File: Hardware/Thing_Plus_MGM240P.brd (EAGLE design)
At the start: 22.9 x 58.4 mm, 172 parts, among them J1 THING_PLUS_LOGICAL, J2 USB Female Type C Connector, J3 QWIIC_RIGHT_ANGLE, J5 MICRO-SDFRICTION, Q1 20V/4.2A/52mΩ/1.4W, U1 MGM240P, U2 XC6222B331MR-G, U3 EFM32GG12B410F1024GL120, U4 MCP73831, U5 MAX17048, U6 M24C02-FMC6TG, U7 MX25R8035FZUIL0, Y1 CRYSTAL-48MHZ

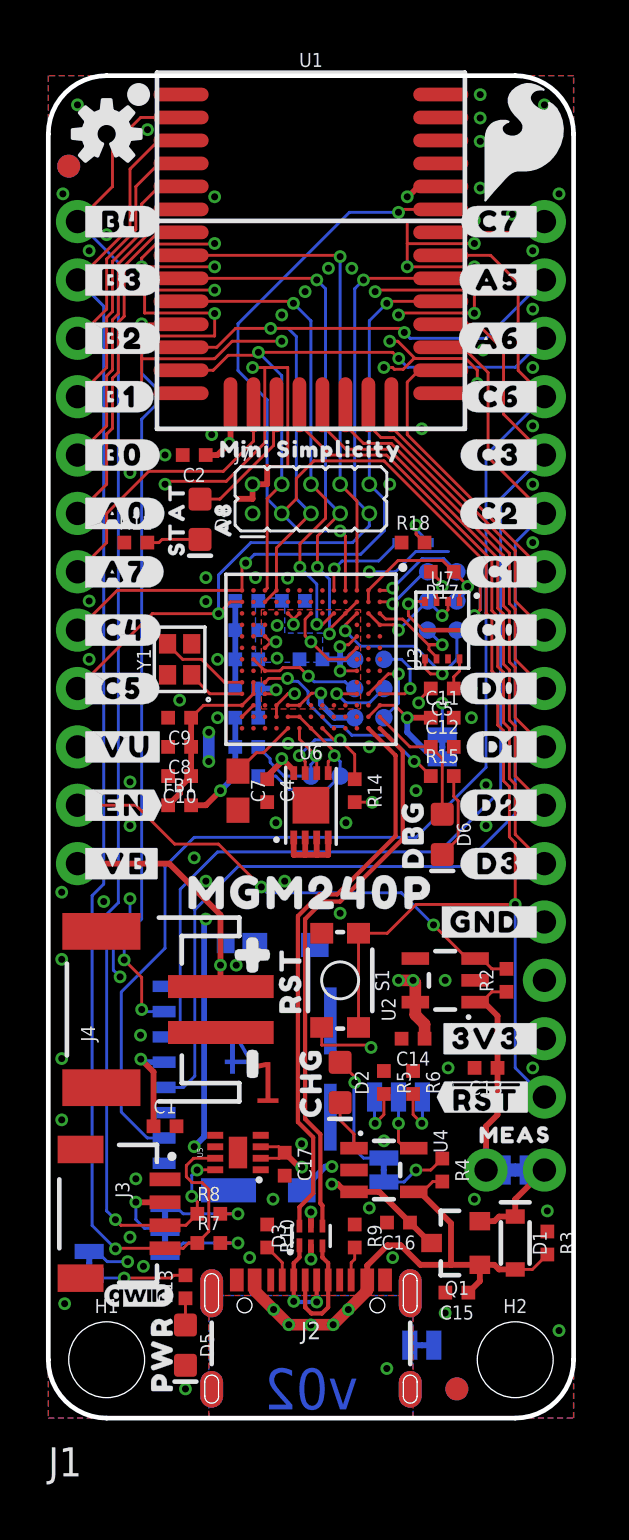
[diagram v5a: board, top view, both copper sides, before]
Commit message: Swap PA04 and PA07
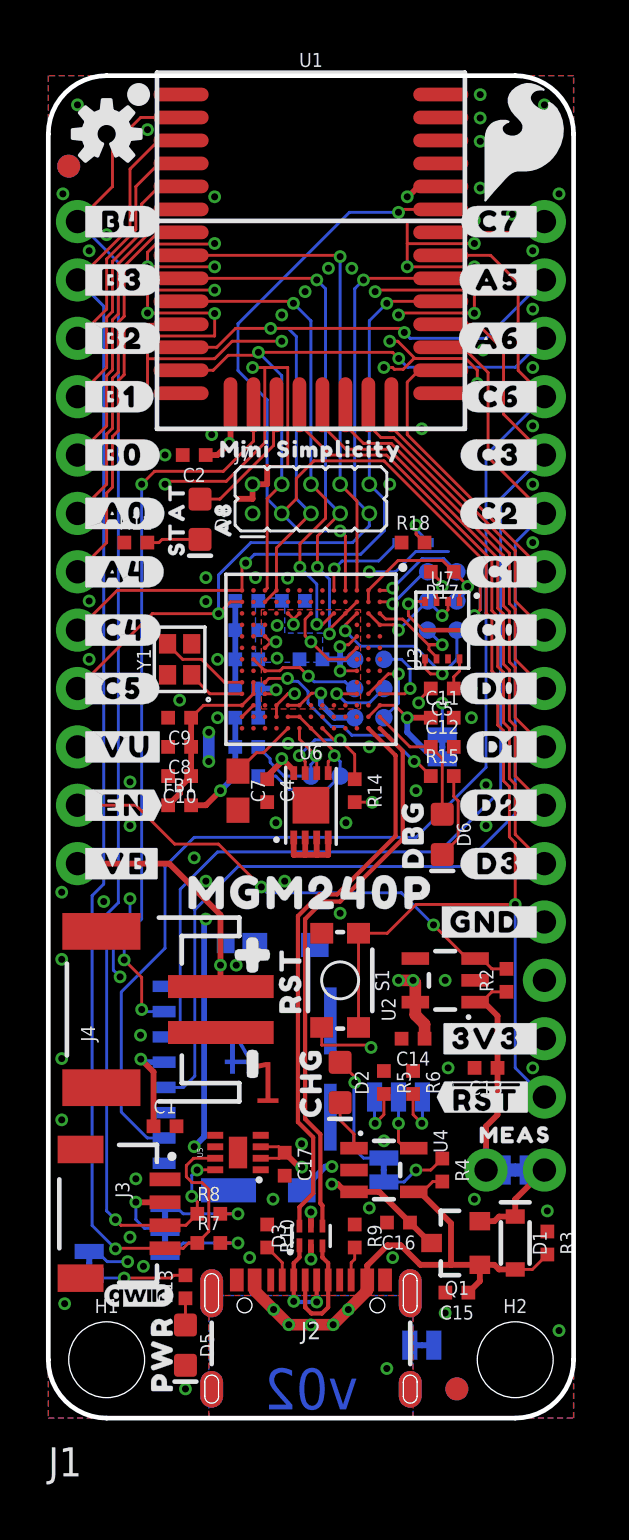
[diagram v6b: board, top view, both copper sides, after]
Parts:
- U$50: device output:#A7_#0 -> output:#A4_#0
- U$8: device output:#_A7#0 -> output:#_A4#0
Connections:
- removed net PA07: J1.7, U1.16
- new net !SD_CS!/PA07: J5.2, U1.16
- net PA04: now also J1.7; no longer J5.2
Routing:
- net !SD_CS!/PA07: track 0.00 -> 31.7 mm, vias 0 -> 3
- net PA04: track 33.7 -> 14.0 mm, vias 3 -> 0
- net PA07: track 12.3 -> 0.00 mm
- net GND: track 120.9 -> 119.9 mm, vias 114 -> 115
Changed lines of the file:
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@@
 <element name="U$6" library="output" package="#_B0#0" value="" x="1.27" y="41.91" smashed="yes"/>
 <element name="U$7" library="output" package="#_A0#0" value="" x="1.27" y="39.37" smashed="yes"/>
-<element name="U$8" library="output" package="#_A7#0" value="" x="1.27" y="36.83" smashed="yes"/>
 <element name="U$9" library="output" package="#_C5#0" value="" x="1.27" y="31.75" smashed="yes"/>
 <element name="U$10" library="output" package="#_C4#0" value="" x="1.27" y="34.29" smashed="yes"/>
@@
 <element name="U$48" library="output" package="#C4_#0" value="" x="1.27" y="34.29" smashed="yes" rot="MR0"/>
 <element name="U$49" library="output" package="#C5_#0" value="" x="1.27" y="31.75" smashed="yes" rot="MR0"/>
-<element name="U$50" library="output" package="#A7_#0" value="" x="1.27" y="36.83" smashed="yes" rot="MR0"/>
 <element name="U$51" library="output" package="#A0_#0" value="" x="1.27" y="39.37" smashed="yes" rot="MR0"/>
 <element name="U$52" library="output" package="#B0_#0" value="" x="1.27" y="41.91" smashed="yes" rot="MR0"/>
@@
 </element>
 <element name="U$33" library="output" package="#LP#0" value="" x="16.51" y="29.21" smashed="yes" rot="MR0"/>
+<element name="U$8" library="output" package="#_A4#0" value="" x="1.27" y="36.83" smashed="yes"/>
+<element name="U$50" library="output" package="#A4_#0" value="" x="1.27" y="36.83" smashed="yes" rot="MR0"/>
 </elements>
 <signals>
@@
 <via x="18.542" y="51.1175" extent="1-16" drill="0.3048"/>
 <via x="21.082" y="50.8" extent="1-16" drill="0.3048"/>
-<via x="4.064" y="50.1015" extent="1-16" drill="0.3048"/>
+<via x="4.318" y="50.1015" extent="1-16" drill="0.3048"/>
 <via x="4.318" y="56.0705" extent="1-16" drill="0.3048"/>
 <via x="2.54" y="51.4985" extent="1-16" drill="0.3048"/>
@@
 <wire x1="18.518" y1="52.1095" x2="18.542" y2="52.1335" width="0.127" layer="1"/>
 <wire x1="18.518" y1="52.1095" x2="15.621" y2="52.1095" width="0.127" layer="1"/>
-<wire x1="7.239" y1="50.1015" x2="4.064" y2="50.1015" width="0.127" layer="1"/>
+<wire x1="7.239" y1="50.1015" x2="4.318" y2="50.1015" width="0.127" layer="1"/>
 <wire x1="7.239" y1="49.0855" x2="7.234" y2="49.0905" width="0.127" layer="1"/>
-<wire x1="7.234" y1="49.0905" x2="4.191" y2="49.0905" width="0.127" layer="1"/>
+<wire x1="7.234" y1="49.0905" x2="4.318" y2="49.0905" width="0.127" layer="1"/>
 <wire x1="7.239" y1="48.0695" x2="7.218" y2="48.0905" width="0.127" layer="1"/>
-<wire x1="7.218" y1="48.0905" x2="4.191" y2="48.0905" width="0.127" layer="1"/>
+<wire x1="7.218" y1="48.0905" x2="4.318" y2="48.0905" width="0.127" layer="1"/>
 <wire x1="7.239" y1="51.1175" x2="7.212" y2="51.0905" width="0.127" layer="1"/>
 <wire x1="7.212" y1="51.0905" x2="4.67683125" y2="51.0905" width="0.127" layer="1"/>
-<wire x1="4.67683125" y1="51.0905" x2="4.064" y2="50.47766875" width="0.127" layer="1"/>
-<wire x1="4.064" y1="50.47766875" x2="4.064" y2="50.1015" width="0.127" layer="1"/>
+<wire x1="4.67683125" y1="51.0905" x2="4.318" y2="50.73166875" width="0.127" layer="1"/>
+<wire x1="4.318" y1="50.73166875" x2="4.318" y2="50.1015" width="0.127" layer="1"/>
 <wire x1="15.21045625" y1="46.863" x2="14.859" y2="46.863" width="0.127" layer="1"/>
 <wire x1="18.669" y1="45.0215" x2="18.669" y2="45.60466875" width="0.127" layer="1"/>
@@
 <wire x1="8.89" y1="40.005" x2="8.89" y2="40.64" width="0.254" layer="1"/>
 <wire x1="8.255" y1="40.005" x2="8.89" y2="40.005" width="0.254" layer="1"/>
-<wire x1="4.191" y1="48.0905" x2="4.191" y2="49.0905" width="0.127" layer="1"/>
 <contactref element="S1" pad="2"/>
 <contactref element="S1" pad="1"/>
@@
 <via x="21.082" y="15.24" extent="1-16" drill="0.3048"/>
 <via x="3.556" y="22.606" extent="1-16" drill="0.3048"/>
-<via x="3.556" y="41.148" extent="1-16" drill="0.3048"/>
 <via x="3.556" y="25.781" extent="1-16" drill="0.3048"/>
 <via x="3.556" y="27.686" extent="1-16" drill="0.3048"/>
@@
 <wire x1="13.06" y1="33.65" x2="13.43" y2="34.02" width="0.127" layer="1"/>
 <wire x1="7.239" y1="48.0695" x2="7.239" y2="47.0905" width="0.127" layer="1"/>
-<wire x1="7.239" y1="47.0905" x2="4.064" y2="47.0905" width="0.127" layer="1"/>
-<wire x1="4.064" y1="47.0905" x2="4.064" y2="46.101" width="0.127" layer="1"/>
+<wire x1="7.239" y1="47.0905" x2="4.318" y2="47.0905" width="0.127" layer="1"/>
+<wire x1="4.318" y1="47.0905" x2="4.318" y2="46.101" width="0.127" layer="1"/>
 <contactref element="U7" pad="EPAD"/>
 <contactref element="U7" pad="4"/>
@@
 <via x="12.7" y="21.971" extent="1-16" drill="0.3048"/>
 <via x="18.542" y="34.925" extent="1-16" drill="0.3048"/>
-<wire x1="7.239" y1="46.101" x2="4.064" y2="46.101" width="0.127" layer="1"/>
-<wire x1="4.064" y1="44.6405" x2="4.064" y2="46.101" width="0.127" layer="1"/>
+<wire x1="7.239" y1="46.101" x2="4.318" y2="46.101" width="0.127" layer="1"/>
+<wire x1="4.318" y1="46.101" x2="4.318" y2="44.8945" width="0.127" layer="1"/>
+<wire x1="4.064" y1="44.6405" x2="4.318" y2="44.8945" width="0.127" layer="1"/>
 <wire x1="10.16" y1="46.863" x2="8.001" y2="46.863" width="0.127" layer="1"/>
 <wire x1="8.001" y1="46.863" x2="7.239" y2="46.101" width="0.127" layer="1"/>
@@
 <wire x1="18.542" y1="34.925" x2="18.796" y2="35.179" width="0.127" layer="16"/>
 <wire x1="18.796" y1="35.179" x2="18.796" y2="37.084" width="0.127" layer="16"/>
+<via x="4.318" y="48.0905" extent="1-16" drill="0.3048"/>
+<wire x1="4.318" y1="49.0905" x2="4.318" y2="48.0905" width="0.127" layer="1"/>
+<via x="4.318" y="47.0905" extent="1-16" drill="0.3048"/>
 </signal>
 <signal name="3.3V">
@@
 <signal name="PA04">
 <contactref element="U1" pad="11"/>
-<contactref element="J5" pad="2"/>
-<wire x1="4.064" y1="19.177" x2="4.064" y2="17.78" width="0.127" layer="1"/>
-<wire x1="4.064" y1="19.177" x2="3.302" y2="19.939" width="0.127" layer="1"/>
-<via x="4.064" y="17.78" extent="1-16" drill="0.3048"/>
-<wire x1="4.064" y1="17.78" x2="4.154" y2="17.69" width="0.127" layer="16"/>
-<wire x1="4.154" y1="17.69" x2="5.04" y2="17.69" width="0.127" layer="16"/>
-<wire x1="4.064" y1="21.717" x2="3.302" y2="20.955" width="0.127" layer="16"/>
-<wire x1="3.302" y1="20.955" x2="3.302" y2="19.939" width="0.127" layer="16"/>
-<via x="3.302" y="19.939" extent="1-16" drill="0.3048"/>
-<wire x1="4.064" y1="43.46795625" x2="4.064" y2="21.717" width="0.127" layer="16"/>
-<wire x1="4.064" y1="43.46795625" x2="4.6609" y2="44.06485625" width="0.127" layer="16"/>
-<wire x1="4.6609" y1="44.8647" x2="4.064" y2="45.4616" width="0.127" layer="16"/>
-<wire x1="4.064" y1="45.4616" x2="4.064" y2="47.6206" width="0.127" layer="16"/>
-<via x="4.064" y="47.6206" extent="1-16" drill="0.3048"/>
-<wire x1="4.064" y1="47.6206" x2="5.7594" y2="47.6206" width="0.127" layer="1"/>
-<wire x1="5.7594" y1="47.6206" x2="5.78" y2="47.6" width="0.127" layer="1"/>
-<wire x1="4.6609" y1="44.06485625" x2="4.6609" y2="44.8647" width="0.127" layer="16"/>
+<contactref element="J1" pad="7"/>
+<wire x1="5.78" y1="47.6" x2="3.531" y2="47.6" width="0.127" layer="1"/>
+<wire x1="3.531" y1="47.6" x2="3.302" y2="47.371" width="0.127" layer="1"/>
+<wire x1="3.302" y1="47.371" x2="3.302" y2="45.4043625" width="0.127" layer="1"/>
+<wire x1="3.302" y1="45.4043625" x2="3.048" y2="45.1503625" width="0.127" layer="1"/>
+<wire x1="3.048" y1="42.969575" x2="2.794" y2="42.715575" width="0.127" layer="1"/>
+<wire x1="2.794" y1="40.513" x2="2.54" y2="40.259" width="0.127" layer="1"/>
+<wire x1="2.54" y1="40.259" x2="2.54" y2="38.1" width="0.127" layer="1"/>
+<wire x1="2.54" y1="38.1" x2="1.27" y2="36.83" width="0.127" layer="1"/>
+<wire x1="3.048" y1="45.1503625" x2="3.048" y2="42.969575" width="0.127" layer="1"/>
+<wire x1="2.794" y1="42.715575" x2="2.794" y2="40.513" width="0.127" layer="1"/>
 </signal>
 <signal name="!DBG_RESET!">
@@
 <wire x1="15.24" y1="31.115" x2="14.605" y2="30.48" width="0.127" layer="16"/>
 </signal>
-<signal name="PA07">
-<contactref element="J1" pad="7"/>
+<signal name="!SD_CS!/PA07">
 <contactref element="U1" pad="16"/>
-<wire x1="2.54" y1="39.37" x2="2.54" y2="38.1" width="0.127" layer="1"/>
 <wire x1="8.93" y1="42.51346875" x2="7.62013125" y2="41.2036" width="0.127" layer="1"/>
-<wire x1="7.62013125" y1="41.2036" x2="4.3736" y2="41.2036" width="0.127" layer="1"/>
-<wire x1="4.3736" y1="41.2036" x2="2.54" y2="39.37" width="0.127" layer="1"/>
-<wire x1="2.54" y1="38.1" x2="1.27" y2="36.83" width="0.127" layer="1"/>
 <wire x1="8.93" y1="44.1" x2="8.93" y2="42.51346875" width="0.127" layer="1"/>
+<contactref element="J5" pad="2"/>
+<wire x1="4.064" y1="19.177" x2="4.064" y2="17.78" width="0.127" layer="1"/>
+<wire x1="4.064" y1="19.177" x2="3.302" y2="19.939" width="0.127" layer="1"/>
+<via x="4.064" y="17.78" extent="1-16" drill="0.3048"/>
+<wire x1="4.064" y1="17.78" x2="4.154" y2="17.69" width="0.127" layer="16"/>
+<wire x1="4.154" y1="17.69" x2="5.04" y2="17.69" width="0.127" layer="16"/>
+<wire x1="4.064" y1="21.717" x2="3.302" y2="20.955" width="0.127" layer="16"/>
+<wire x1="3.302" y1="20.955" x2="3.302" y2="19.939" width="0.127" layer="16"/>
+<via x="3.302" y="19.939" extent="1-16" drill="0.3048"/>
+<wire x1="4.6276" y1="41.2036" x2="4.064" y2="40.64" width="0.127" layer="1"/>
+<via x="4.064" y="40.64" extent="1-16" drill="0.3048"/>
+<wire x1="7.62013125" y1="41.2036" x2="4.6276" y2="41.2036" width="0.127" layer="1"/>
+<wire x1="4.064" y1="40.64" x2="4.064" y2="21.717" width="0.127" layer="16"/>
 </signal>
 <signal name="N$1">

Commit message: Design review updates
Add GND vias along antenna cutout edge
Add extra GND vias near MGM240P GND pads
Add pullup resistor to SD card CS pin
Add extra GND vias between I2C and SPI traces on bottom
Widen DECOUPLE trace
Add series resistors to MGM240P's RX inputs to prevent contention between debugger, Mini Simplicity connector, and Thing Plus RX pin
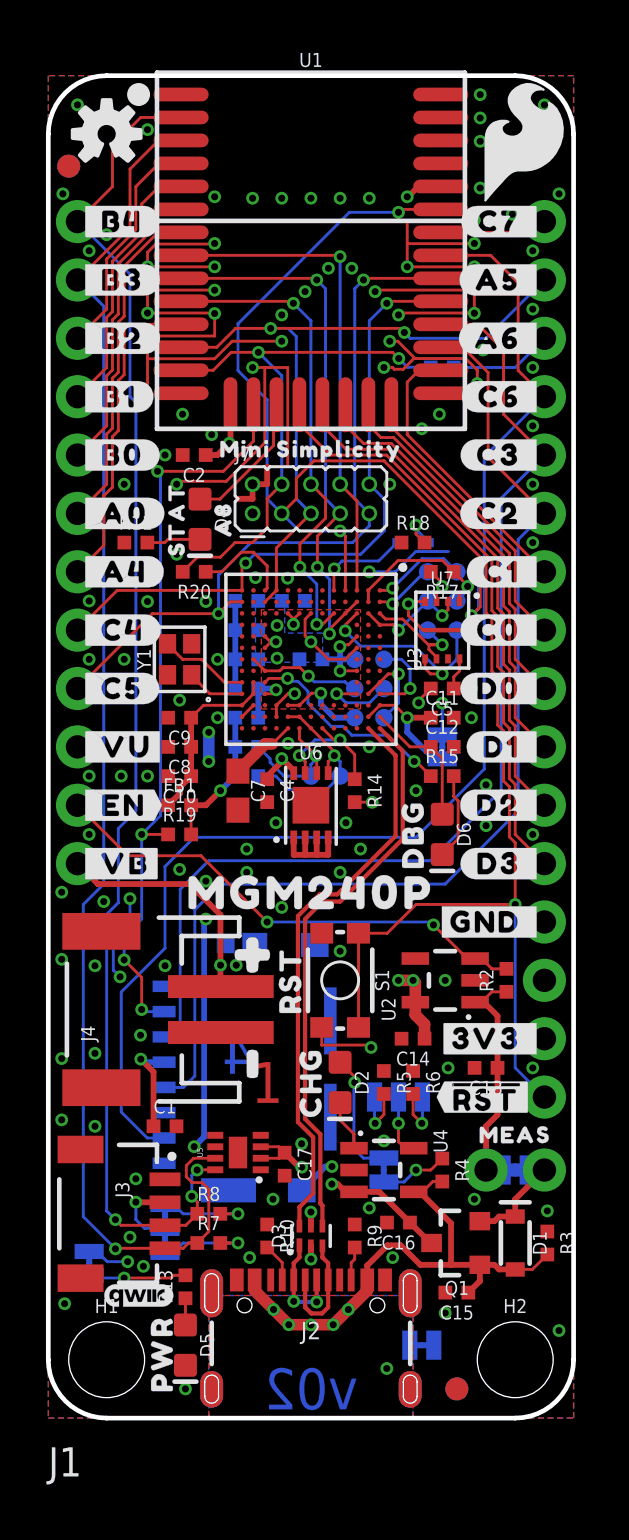
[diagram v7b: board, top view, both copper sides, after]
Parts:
- added R19: 100k, SparkFun-Resistors:0402-TIGHT
- added R20, R21: 330, SparkFun-Resistors:0402-TIGHT
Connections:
- new net N$25: R20.1, U3.L1
- new net N$26: J1.15, R21.1
- net !SD_CS!/PA07: now also R19.1
- net 3.3V: now also R19.2
- net RX/PA06: now also R20.2, R21.2; no longer J1.15, U3.L1
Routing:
- net N$26: track 0.00 -> 4.47 mm
- net N$25: track 0.00 -> 4.38 mm
- net RX/PA06: track 28.0 -> 24.3 mm
- net 3.3V: track 37.7 -> 39.0 mm
- net !SD_CS!/PA07: track 31.7 -> 32.9 mm, vias 3 -> 4
- net SDA/PB04: track 58.7 -> 59.4 mm
- net GND: track 119.9 -> 119.5 mm, vias 115 -> 136
